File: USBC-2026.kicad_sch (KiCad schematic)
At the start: 29 parts, among them J1 USB_C_Receptacle, U1 TPS25762CQRQLRQ1

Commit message: Updated IC again; imported new symbols and footprints.
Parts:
- removed C10, C11: 300p, Package_TO_SOT_SMD:SOT-23-5, symbol Device:C
- removed C12, C13, C8, C9: C, Package_TO_SOT_SMD:SOT-23-5, symbol Device:C
- removed C14: 1n, Package_TO_SOT_SMD:SOT-23-5, symbol Device:C
- removed C15: 3.3n, Package_TO_SOT_SMD:SOT-23-5, symbol Device:C
- removed R10, R11, R8, R9: 2.2, Resistor_THT:R_Array_SIP4, symbol Device:R_US
- removed R2: 10, Resistor_THT:R_Array_SIP4, symbol Device:R_US
- removed R3: 0, Resistor_THT:R_Array_SIP4, symbol Device:R_US
- removed R4, R5, R6, R7: R_US, Resistor_THT:R_Array_SIP4, symbol Device:R_US
- removed U1: TPS25762CQRQLRQ1, RQL0029A-MFG, symbol symbol_library:TPS25762CQRQLRQ1
- added IC1: TPS25752ASRSMR, QFN40P400X400X100-33N-D, symbol symbol_library:TPS25752ASRSMR
- added U1: TPS55288RPMR, VQFN-HR26_RPM_TEX, symbol symbol_library:TPS55288RPMR
- C1: value C -> 330p; footprint Package_TO_SOT_SMD:SOT-23-5 -> (none)
- C2: value 30u -> 330p; footprint Package_TO_SOT_SMD:SOT-23-5 -> (none)
- C3: value 0.22u -> 0.1u; footprint Package_TO_SOT_SMD:SOT-23-5 -> (none)
- C4: value 0.2u -> 0.1u; footprint Package_TO_SOT_SMD:SOT-23-5 -> (none)
- C5: value 130u -> 22u; footprint Package_TO_SOT_SMD:SOT-23-5 -> (none)
- C6: value 22u -> 10u; footprint Package_TO_SOT_SMD:SOT-23-5 -> (none)
- C7: value 0.2u -> 4.7u; footprint Package_TO_SOT_SMD:SOT-23-5 -> (none)
- R1: footprint Resistor_THT:R_Array_SIP4 -> (none)
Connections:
- net +12V: now also IC1.19 (VSYS), U1.3 (VIN); no longer C7.1
- net CC1: now also C2.1, IC1.24 (CC1)
- net CC2: now also C1.1, IC1.25 (CC2)
- net GND: now also C5.1, C7.1, IC1.11 (GND_1), IC1.12 (GND_2), IC1.14 (GND_3), U1.10 (AGND), U1.9 (PGND); no longer C4.2, C5.2, C7.2
- net at C3.2: now also L1.2, U1.23 (SW1)
- net Vbus: now reaches J1.A4 (VBUS), J1.A9 (VBUS), J1.B4 (VBUS), J1.B9 (VBUS)
- net Vbus: now also R1.1; no longer C5.1, R1.2
- net at L1.1: now also C4.2, U1.25 (SW2)
- net at C3.1: now also U1.22 (BOOT1)
- net DM: no longer names the net of J1.A7 (D-)
- net DM: no longer J1.B7 (D-)
- net DP: no longer names the net of J1.A6 (D+)
- net DP: no longer J1.B6 (D+)
- new net: C5.2, R1.2, U1.11 (VOUT)
- new net: C7.2, U1.19 (VCC)
- new net: C4.1, U1.20 (BOOT2)
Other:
- note added: "**Mosfets**"

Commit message: Continued work on DC/DC and USB PD Circuits.
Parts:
- added C8: 0.01u, symbol Device:C
- added R2: 20k, symbol Device:R_US
- added R3: 49.9k, symbol Device:R_US
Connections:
- net GND: now also IC1.13 (GPIO11), IC1.18 (GPIO3), IC1.30 (GPIO7), IC1.31 (GPIO6), IC1.6 (GPIO1), C8.2, R2.1, R3.2
- net D_P: now reaches J1.A6 (D+)
- net D_P: now also IC1.22 (GPIO4/USB_P), J1.B6 (D+)
- net D_N: now reaches J1.A7 (D-)
- net D_N: now also IC1.23 (GPIO5/USB_N), J1.B7 (D-)
- net CC_SDA: now reaches IC1.15 (I2CC_SDA)
- net CC_SDA: now also U1.6 (SDA)
- net CC_SLC: now reaches IC1.16 (I2CC_SCL)
- net CC_SLC: now also U1.5 (SCL)
- net at IC1.26 (VBUS_1): now also IC1.27 (VBUS_2)
- net +5V: now reaches IC1.28 (PP5V_1)
- net +5V: now also IC1.29 (PP5V_2)
- net at U1.15 (MODE): now also R2.2
- net at U1.7 (DITH/SYNC): now also C8.1
- net at U1.8 (FSW): now also R3.1
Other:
- note added: "****5V,3A Buck****"
- note added: "**Mosfets** = IHLP5050EZER4R7M5A???? - Would need to recalc components"
- note removed: "**Mosfets**"
- moved on the sheet: C1, C2, C3, C4, C5, C6, C7, IC1, J1, L1, R1, U1

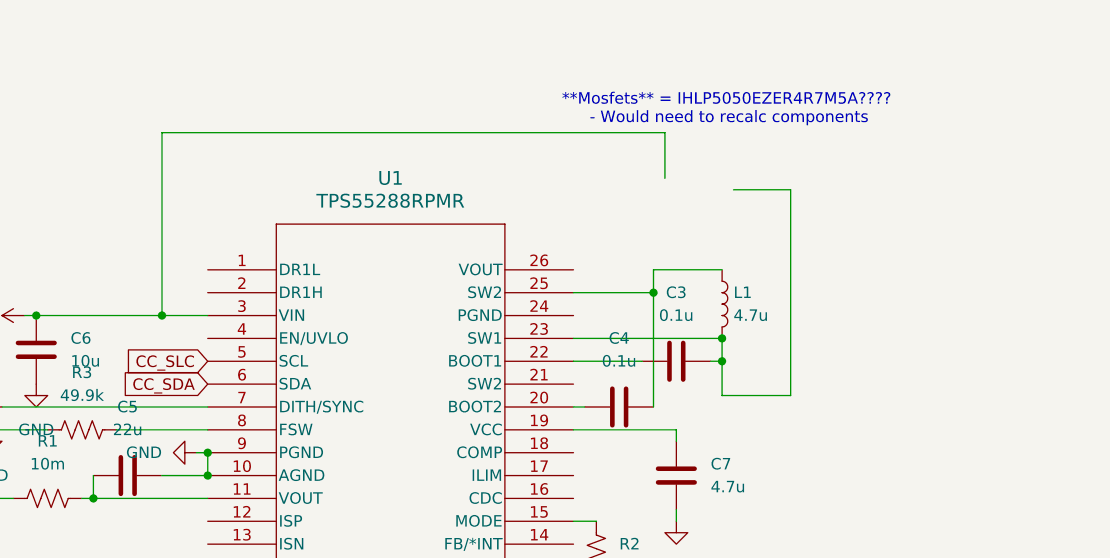
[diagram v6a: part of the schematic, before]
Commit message: Added NMOS Symbols
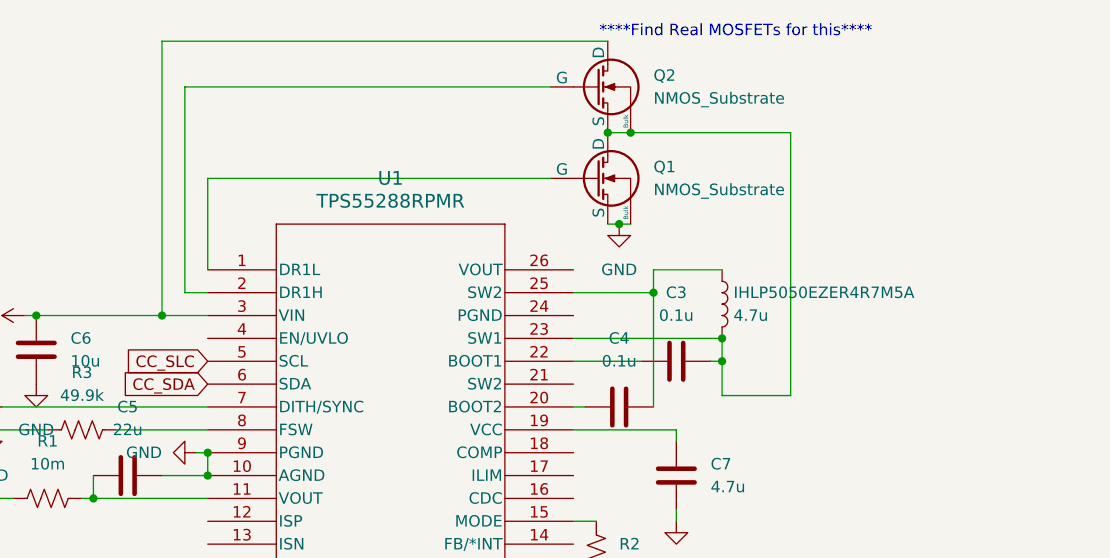
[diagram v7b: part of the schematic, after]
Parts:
- added Q1, Q2: NMOS_Substrate, symbol Simulation_SPICE:NMOS_Substrate
- renumbered L1 to IHLP5050EZER4R7M5A
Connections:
- net +12V: now also Q2.1 (D)
- net GND: now also Q1.3 (S), Q1.4 (Bulk)
- net at C3.2, IHLP5050EZER4R7M5A.2, U1.23 (SW1): now also Q1.1 (D), Q2.3 (S), Q2.4 (Bulk)
- net at U1.1 (DR1L): now also Q1.2 (G)
- net at U1.2 (DR1H): now also Q2.2 (G)
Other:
- note added: "****Find Real MOSFETs for this****"
- note removed: "**Mosfets** = IHLP5050EZER4R7M5A???? - Would need to recalc components"

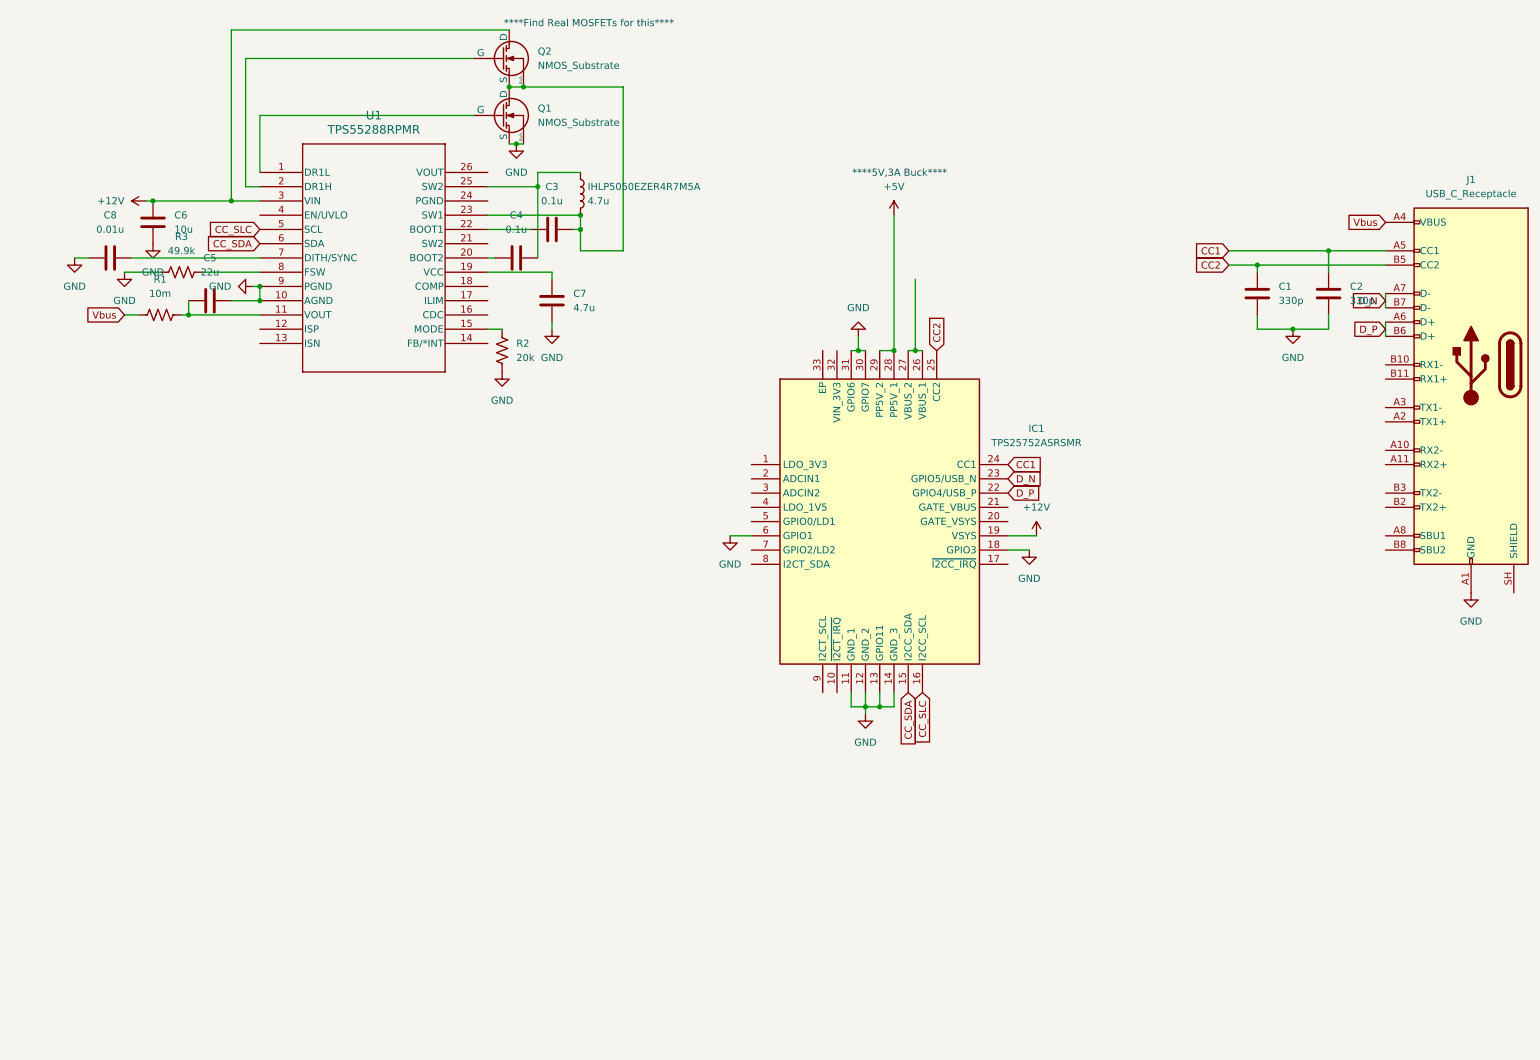
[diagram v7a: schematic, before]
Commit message: Added 5V buck converter supply
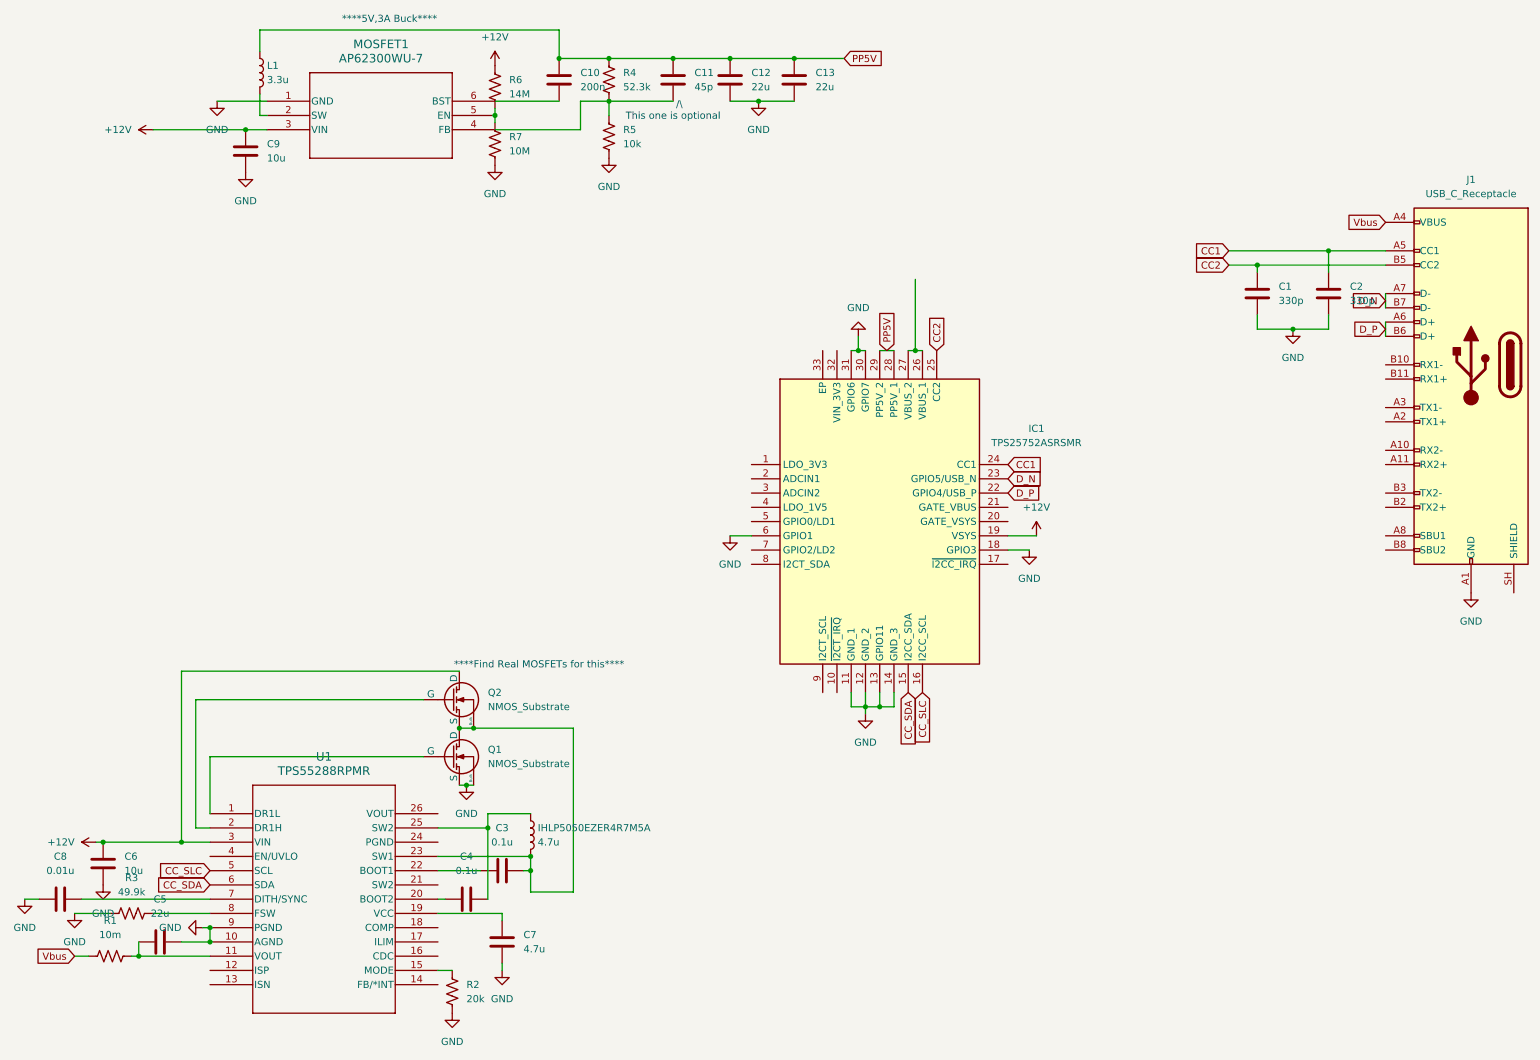
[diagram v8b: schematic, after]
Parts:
- added C10: 200n, symbol Device:C
- added C11: 45p, symbol Device:C
- added C12, C13: 22u, symbol Device:C
- added C9: 10u, symbol Device:C
- added L1: 3.3u, symbol Device:L
- added MOSFET1: AP62300WU-7, TSOT26_DIO, symbol symbol_library:AP62300WU-7
- added R4: 52.3k, symbol Device:R_US
- added R5: 10k, symbol Device:R_US
- added R6: 14M, symbol Device:R_US
- added R7: 10M, symbol Device:R_US
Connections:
- net +12V: now also C9.2, MOSFET1.3 (VIN), R6.1
- net GND: now also C12.1, C13.1, C9.1, MOSFET1.1 (GND), R5.2, R7.2
- net +5V renamed PP5V
- net PP5V: now also C10.2, C11.2, C12.2, C13.2, L1.1, R4.1
- new net: C11.1, MOSFET1.4 (FB), R4.2, R5.1
- new net: MOSFET1.5 (EN), R6.2, R7.1
- new net: C10.1, MOSFET1.6 (BST)
- new net: L1.2, MOSFET1.2 (SW)
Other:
- note added: "/\ This one is optional"
- moved on the sheet: C3, C4, C5, C6, C7, C8, IHLP5050EZER4R7M5A, Q1, Q2, R1, R2, R3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
